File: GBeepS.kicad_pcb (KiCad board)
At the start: 4 copper layers, 10 x 12 mm, 35 parts, among them J1 Ant, U1 NCP160xMX, U2 MMC3416xPJ, U3 ZOE-M8Q, U4 EFM8BB51F16G-A-QFN20, Y1 ECS-.327-7-16-TR3

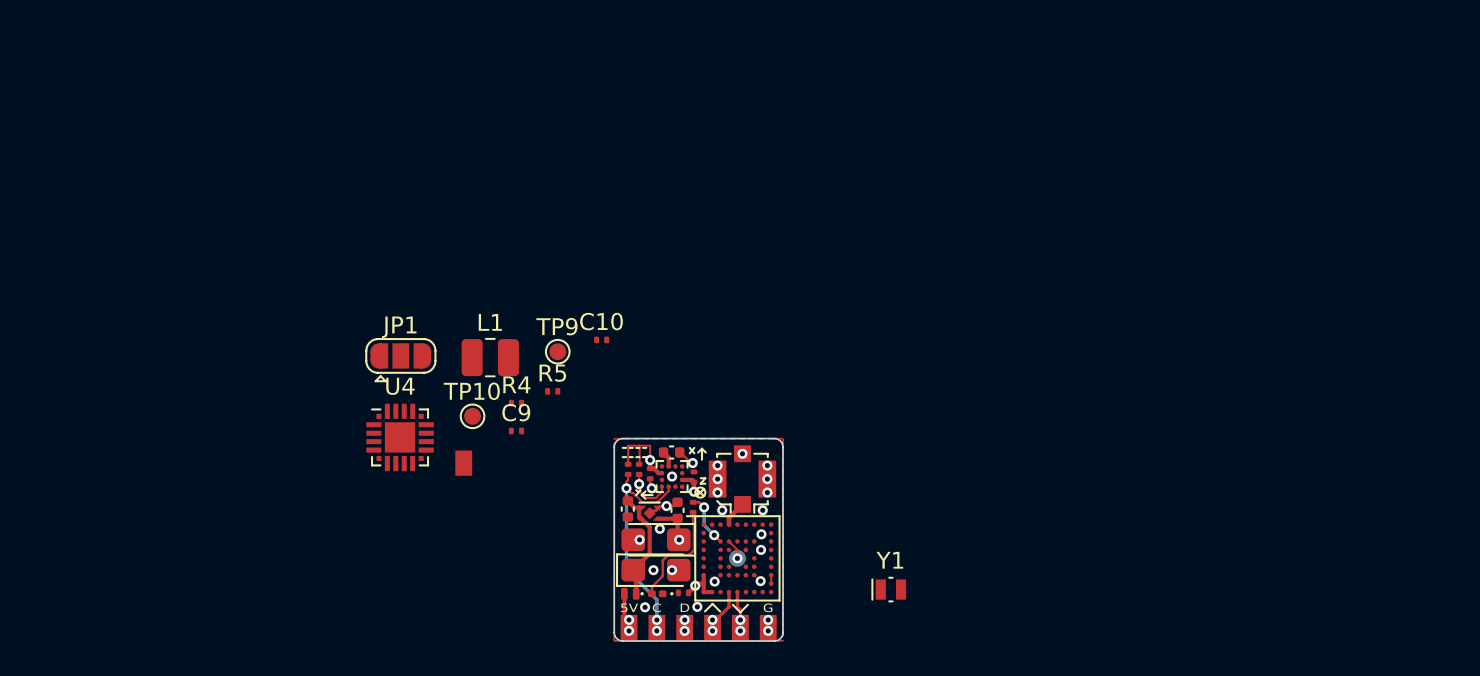
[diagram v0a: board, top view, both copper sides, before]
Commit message: rudimentary layout and 3D models
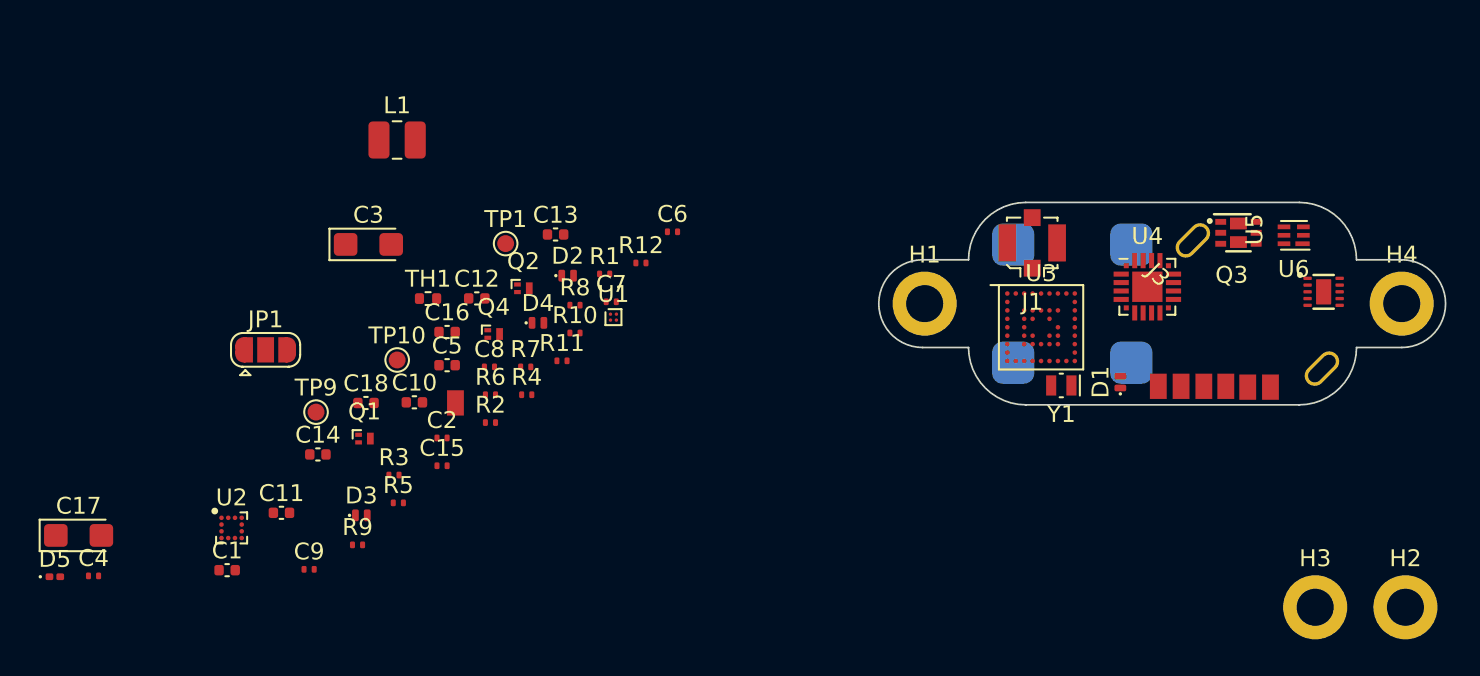
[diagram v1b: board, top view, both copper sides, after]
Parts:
- added C11: 10µF, Capacitor_SMD:C_0402_1005Metric, F.Cu at (80.3, 104.4)
- added C12: 10µF, Capacitor_SMD:C_0402_1005Metric, F.Cu at (91.8, 91.7)
- added C13: 10µF, Capacitor_SMD:C_0402_1005Metric, F.Cu at (96.5, 87.9)
- added C14: 10µF, Capacitor_SMD:C_0402_1005Metric, F.Cu at (82.4, 100.9)
- added C15: 100nF, Yolo-GPS:C_0201_0603Metric_mod, F.Cu at (89.8, 101.6)
- added C16: 10µF, Capacitor_SMD:C_0402_1005Metric, F.Cu at (90.1, 93.7)
- added C17: 100µF, Capacitor_Tantalum_SMD:CP_EIA-3216-18_Kemet-A, F.Cu at (68.2, 105.7)
- added C18: 10µF, Capacitor_SMD:C_0402_1005Metric, F.Cu at (85.3, 97.9)
- added D3: CDBQC0130L-HF, Yolo-GPS:D_SOD-932F_0402_1005Metric, F.Cu at (85.0, 104.5)
- added D4: CDBQC0130L-HF, Yolo-GPS:D_SOD-932F_0402_1005Metric, F.Cu at (95.5, 93.1)
- added D5: green, LED_SMD:LED_0201_0603Metric, F.Cu at (66.8, 108.2)
- added H1: MountingHole, MountingHole:MountingHole_2.2mm_M2_DIN965_Pad, F.Cu at (118.4, 92.0)
- added H2: MountingHole, MountingHole:MountingHole_2.2mm_M2_DIN965_Pad, F.Cu at (146.9, 110.0)
- added H3: MountingHole, MountingHole:MountingHole_2.2mm_M2_DIN965_Pad, F.Cu at (141.6, 110.0)
- added H4: MountingHole, MountingHole:MountingHole_2.2mm_M2_DIN965_Pad, F.Cu at (146.7, 92.0)
- added J2: BAT_TAB_POS, MountingHole:MountingHole_2.2mm_M2_DIN965_Pad, B.Cu at (141.9, 95.8)
- added J3: BAT_TAB_NEGATIVE, MountingHole:MountingHole_2.2mm_M2_DIN965_Pad, F.Cu at (134.3, 88.2)
- added LS1: CMT-85853-97-SMT-TR, Buzzer_Beeper:MagneticBuzzer_CUI_CMT-8504-100-SMT, B.Cu at (127.2, 92.0)
- added Q1: PMZ130UNEYL, Package_DFN_QFN:Diodes_DFN1006-3, F.Cu at (85.2, 100.0)
- added Q2: PMZ130UNEYL, Package_DFN_QFN:Diodes_DFN1006-3, F.Cu at (94.6, 91.1)
- added Q3: DMN1025UFDB, Yolo-GPS:U-DFN2020-6-2EP, F.Cu at (137.0, 87.8)
- added Q4: PMZB320UPE, Package_DFN_QFN:Diodes_DFN1006-3, F.Cu at (92.8, 93.8)
- added R10: 10k, Yolo-GPS:R_0201_0603Metric_mod, F.Cu at (97.7, 93.7)
- added R11: 360R, Yolo-GPS:R_0201_0603Metric_mod, F.Cu at (96.9, 95.4)
- added R12: 300R, Yolo-GPS:R_0201_0603Metric_mod, F.Cu at (101.6, 89.6)
- added R6: 1M, Yolo-GPS:R_0201_0603Metric_mod, F.Cu at (92.7, 97.4)
- added R7: 200k, Yolo-GPS:R_0201_0603Metric_mod, F.Cu at (94.8, 95.8)
- added R8: 100k, Yolo-GPS:R_0201_0603Metric_mod, F.Cu at (97.7, 92.1)
- added R9: 2k2, Yolo-GPS:R_0201_0603Metric_mod, F.Cu at (84.8, 106.3)
- added TH1: NTC 10k, Resistor_SMD:R_0402_1005Metric, F.Cu at (89.0, 91.7)
- added U5: BQ24040, Yolo-GPS:WSON_10_P0.4_2x2, F.Cu at (142.1, 91.3)
- added U6: BQ29700, Package_SON:WSON-6_1.5x1.5mm_P0.5mm, F.Cu at (140.3, 87.9)
- C1: value 1u -> 10µF
- C10: value 1u -> 10µF; footprint Yolo-GPS:C_0201_0603Metric_mod -> Capacitor_SMD:C_0402_1005Metric
- C2: value 1u -> 1µF; footprint Capacitor_SMD:C_0402_1005Metric -> Yolo-GPS:C_0201_0603Metric_mod
- C3: value 100u -> 100µF
- C4, C7, C8, C9: value 1u -> 1µF
- C5: value 4u7 -> 4µ7
- C6: value 100u -> 1nF; footprint Capacitor_Tantalum_SMD:CP_EIA-3216-18_Kemet-A -> Yolo-GPS:C_0201_0603Metric_mod
- D1: value green -> CDBQC0130L-HF; footprint LED_SMD:LED_0201_0603Metric -> Yolo-GPS:D_SOD-932F_0402_1005Metric
- R1: value 360R -> 1M
- R5: value 1k -> 100k
- TP1: moved to F.Cu
- U1: value NCP160xMX -> TCR3UG33A; footprint Yolo-GPS:OnSemi-XDFN-4-1EP_1x1mm_P0.65mm_EP0.52x0.52mm -> Package_BGA:WLP-4_0.73x0.73mm_Layout2x2_P0.35mm_Ball0.22mm_Pad0.2mm_NSMD
- moved U4 45.2 mm to (131.6, 91.0)
- moved TP2 40.6 mm to (138.9, 97.0)
- moved TP4 34.2 mm to (133.6, 96.9)
- moved TP6 33.6 mm to (136.2, 96.9)
- moved C4 33.5 mm to (69.1, 108.1), turned to 0 degrees
- moved TP7 31.8 mm to (137.6, 97.0)
- moved TP3 31.5 mm to (132.2, 96.9)
- moved TP5 31.0 mm to (134.9, 96.9)
- moved D1 30.2 mm to (130.0, 96.7), turned to 90 degrees
- moved U2 26.3 mm to (77.3, 105.3), turned to 0 degrees
- moved C3 24.4 mm to (85.4, 88.5), turned to 0 degrees
- moved C1 24.0 mm to (77.0, 107.8), turned to 0 degrees
- moved TP1 23.2 mm to (93.6, 88.4), turned to 0 degrees
- moved U3 22.6 mm to (125.3, 93.4)
- moved J1 22.2 mm to (124.8, 88.4)
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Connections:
- C1 pad 1: +5V -> BATT_PACK
- C10 pad 1: VSupply_EFM -> VIN
- C6 pad 1: +5V -> BATT_VOL
- C7 pad 1: +3V3 -> Net-(C7-Pad1)
- D1 pad 1: GND -> BATT_PACK
- D2 pad 1: +5V -> VIN
- JP1 pad 3: VSupply_EFM -> +3V3
- R1 pad 1: Net-(R1-Pad1) -> GND
- R1 pad 2: Net-(D1-Pad2) -> Net-(D2-Pad2)
- R4 pad 1: VSupply_EFM -> +3V3
- U3 pad P$C3: Net-(R1-Pad1) -> timepulse
- U3 pad P$H9: VBackup -> +3V3
- U3 pad P$J1: +3V3 -> Net-(C7-Pad1)
- U3 pad P$J2: +3V3 -> Net-(C7-Pad1)
- U4 pad 10: unconnected-(U4-Pad10) -> BATT_VOL
- U4 pad 11: unconnected-(U4-Pad11) -> EN_BATT_VOL
- U4 pad 14: unconnected-(U4-Pad14) -> power_detect
- U4 pad 15: unconnected-(U4-Pad15) -> Net-(U4-Pad15)
- U4 pad 18: unconnected-(U4-Pad18) -> timepulse
- U4 pad 4: VSupply_EFM -> +3V3
- U4 pad 7: unconnected-(U4-Pad7) -> PG
- U4 pad 8: unconnected-(U4-Pad8) -> CHG
- U4 pad 9: unconnected-(U4-Pad9) -> EN_GPA_PWR
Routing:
- net SDA: track 13.7 -> 0.00 mm, vias 3 -> 0
- net SCL: track 13.4 -> 0.00 mm, vias 3 -> 0
- net +3V3: track 12.1 -> 0.00 mm, vias 4 -> 0
- net +5V: track 6.79 -> 0.00 mm
- net Net-(D1-Pad2): track 6.61 -> 0.00 mm
- net GND: track 3.55 -> 0.00 mm, vias 25 -> 0
- net Net-(R1-Pad1): track 3.20 -> 0.00 mm, vias 2 -> 0
- net GNSS_Rx: track 2.82 -> 0.00 mm, vias 2 -> 0
- net Net-(D2-Pad2): track 2.48 -> 0.00 mm, vias 2 -> 0
- net GNSS_Tx: track 2.37 -> 0.00 mm, vias 2 -> 0
- net Net-(J1-Pad1): track 1.53 -> 0.00 mm
- net Net-(TP1-Pad1): track 1.21 -> 0.00 mm, vias 1 -> 0
- net Net-(C5-Pad1): track 0.95 -> 0.00 mm
- net unconnected-(U3-PadP$G9): track 0.50 -> 0.00 mm
- removed copper zone on In2.Cu, net +3V3
- removed copper zone on B.Cu, net GND
- removed copper zone on F.Cu, net GND
- removed copper zone on In1.Cu, net GND
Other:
- board size 10 x 12 mm -> 33.6 x 12 mm
- board text removed: "5V"
- board text removed: "C"
- board text removed: "D"
- board text removed: "G"
- board text removed: "HypaLoc"
- board text removed: "Rev 1.0"
- board text removed: "crteensy"
- board text removed: "safe boot"

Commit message: update layout
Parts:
- TP1: moved to B.Cu
- U1: footprint Package_BGA:WLP-4_0.73x0.73mm_Layout2x2_P0.35mm_Ball0.22mm_Pad0.2mm_NSMD -> Yolo-GPS:WLP-4_0.73x0.73mm_Layout2x2_P0.35mm_Ball0.22mm_Pad0.2mm_NSMD_mod
- moved C17 71.6 mm to (139.0, 94.6), turned to 180 degrees
- moved D5 65.6 mm to (126.8, 81.7)
- moved R9 60.2 mm to (142.2, 88.2), turned to 90 degrees
- moved C18 55.0 mm to (139.5, 88.8), turned to 90 degrees
- moved C1 54.9 mm to (130.6, 95.3)
- moved TH1 54.5 mm to (143.4, 92.6), turned to 90 degrees
- moved C10 53.0 mm to (140.7, 90.9)
- moved C16 52.5 mm to (142.5, 90.9), turned to 180 degrees
- moved C15 52.3 mm to (140.6, 89.3)
- moved TP9 51.6 mm to (133.9, 100.7)
- moved C3 51.3 mm to (136.7, 91.0)
- moved JP1 50.2 mm to (128.7, 103.9)
- moved TP10 49.6 mm to (136.3, 101.2)
- moved D3 47.8 mm to (131.7, 94.2), turned to -90 degrees
- moved Q1 47.1 mm to (130.7, 87.8)
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
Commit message: started routing
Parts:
- removed C8: 1µF, Yolo-GPS:C_0201_0603Metric_mod
- removed H2, H3: MountingHole, MountingHole:MountingHole_2.2mm_M2_DIN965_Pad
- removed JP1: SolderJumper_3_Open, Jumper:SolderJumper-3_P1.3mm_Open_RoundedPad1.0x1.5mm
- added Q5: PMZB320UPE, Package_DFN_QFN:Diodes_DFN1006-3, F.Cu at (127.5, 89.2)
- C7, C9: value 1µF -> 10µF; footprint Yolo-GPS:C_0201_0603Metric_mod -> Capacitor_SMD:C_0402_1005Metric
- L1: value L_Small -> MCHK1608T1R5MKN; footprint Inductor_SMD:L_1008_2520Metric -> Inductor_SMD:L_0603_1608Metric
- TP10, TP9: moved to B.Cu
- moved R3 56.2 mm to (129.8, 87.5), turned to -90 degrees
- moved R2 55.5 mm to (130.1, 88.7), turned to 90 degrees
- moved C4 49.7 mm to (128.4, 86.7), turned to 180 degrees
- moved C5 46.7 mm to (127.0, 87.8), turned to 90 degrees
- moved U2 46.5 mm to (128.4, 87.8), turned to -90 degrees
- moved C14 20.2 mm to (136.2, 94.4), turned to 90 degrees
- moved C13 19.8 mm to (135.3, 94.4), turned to -90 degrees
- moved C12 19.4 mm to (134.5, 94.4), turned to 90 degrees
- moved C11 19.2 mm to (133.7, 94.4), turned to -90 degrees
- moved TP10 17.7 mm to (126.0, 86.8), turned to -90 degrees
- moved TP9 15.3 mm to (127.6, 86.8), turned to -90 degrees
- moved R11 10.8 mm to (132.7, 88.0), turned to 90 degrees
- moved D5 8.08 mm to (133.0, 86.8), turned to 180 degrees
- moved Q4 5.77 mm to (124.2, 97.0), turned to 180 degrees
- moved C9 3.10 mm to (122.6, 93.2), turned to 90 degrees
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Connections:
- C4 pad 1: +3V3 -> Net-(C4-Pad1)
- LS1 pad 3: (no net) -> GND
- LS1 pad 4: (no net) -> GND
- U2 pad 12: +3V3 -> Net-(C4-Pad1)
- U2 pad 6: +3V3 -> Net-(C4-Pad1)
- U4 pad 1: Net-(JP1-Pad2) -> unconnected-(U4-Pad1)
- U4 pad 13: unconnected-(U4-Pad13) -> PG
- U4 pad 14: power_detect -> CHG
- U4 pad 17: unconnected-(U4-Pad17) -> SCL
- U4 pad 18: timepulse -> EN_PWR_MAG
- U4 pad 19: unconnected-(U4-Pad19) -> Buzz_out
- U4 pad 20: Buzz_out -> SDA
- U4 pad 7: PG -> timepulse
- U4 pad 8: CHG -> power_detect
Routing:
- net GND: track 0.00 -> 29.6 mm, vias 0 -> 39
- net SDA: track 0.00 -> 15.5 mm, vias 0 -> 2
- net BATT_PACK: track 0.00 -> 14.6 mm, vias 0 -> 1
- net SCL: track 0.00 -> 14.4 mm, vias 0 -> 3
- net C2D: track 0.00 -> 14.4 mm, vias 0 -> 1
- net EN_GPA_PWR: track 0.00 -> 13.9 mm, vias 0 -> 2
- net GNSS_Rx: track 0.00 -> 13.9 mm, vias 0 -> 3
- net Net-(D2-Pad2): track 0.00 -> 12.8 mm
- net GNSS_Tx: track 0.00 -> 11.7 mm, vias 0 -> 3
- net +3V3: track 0.00 -> 10.6 mm, vias 0 -> 14
- net Net-(R5-Pad1): track 0.00 -> 8.12 mm
- net timepulse: track 0.00 -> 7.90 mm, vias 0 -> 2
- net C2CK: track 0.00 -> 7.29 mm, vias 0 -> 1
- net BATT_VOL: track 0.00 -> 5.63 mm
- net EN_BATT_VOL: track 0.00 -> 4.60 mm
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- added copper zone on In2.Cu, net +3V3
- added copper zone on In1.Cu, net GND
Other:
- board text added: "C14"

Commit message: added pushbutton and routed everything
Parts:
- added SW1: EVP-AKE31A, Yolo-GPS:EVPAV, F.Cu at (143.0, 87.0)
- moved D1 8.49 mm to (130.7, 95.3), turned to 90 degrees
- moved C6 6.36 mm to (131.6, 88.2), turned to 0 degrees
- moved Q1 6.05 mm to (130.5, 94.0), turned to -90 degrees
- moved TH1 2.34 mm to (142.4, 94.7), turned to 180 degrees
- moved R6 1.96 mm to (132.7, 95.0), turned to -90 degrees
- moved R9 1.77 mm to (140.4, 88.7), turned to -90 degrees
- moved C15 1.73 mm to (138.9, 89.0)
- moved U6 1.68 mm to (139.2, 87.5)
- moved R7 1.35 mm to (137.8, 92.0)
- moved C18 1.20 mm to (139.8, 90.0), turned to 180 degrees
- moved Q3 1.10 mm to (136.7, 87.9)
- moved R1 0.85 mm to (132.7, 93.8), turned to -90 degrees
- moved D3 0.78 mm to (131.7, 94.6), turned to 90 degrees
- moved R12 0.73 mm to (141.3, 89.8), turned to 90 degrees
- moved LS1 0.22 mm to (126.8, 92.1), turned to 180 degrees
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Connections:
- U4 pad 10: BATT_VOL -> power_detect
- U4 pad 16: unconnected-(U4-Pad16) -> SW
- U4 pad 19: Buzz_out -> BATT_VOL
- U4 pad 8: power_detect -> Buzz_out
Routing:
- net BATT_PACK: track 14.6 -> 43.6 mm, vias 1 -> 3
- net EN_PWR_MAG: track 0.00 -> 19.0 mm, vias 0 -> 2
- net VIN: track 0.52 -> 17.8 mm, vias 1 -> 2
- net Net-(C15-Pad1): track 0.00 -> 12.7 mm
- net GND: track 29.6 -> 41.6 mm, vias 39 -> 58
- net CHG: track 0.00 -> 11.9 mm, vias 0 -> 2
- net SW: track 0.00 -> 11.8 mm, vias 0 -> 4
- net BATT_VOL: track 5.63 -> 16.6 mm, vias 0 -> 4
- net PG: track 0.00 -> 8.35 mm, vias 0 -> 2
- net SDA: track 15.5 -> 23.3 mm, vias 2 -> 4
- net TS: track 0.00 -> 4.58 mm
- net Net-(Q3-Pad5): track 0.00 -> 4.31 mm
- net Net-(Q3-Pad3): track 0.00 -> 3.28 mm
- net Net-(Q3-Pad2): track 0.00 -> 3.28 mm
- net Net-(C15-Pad2): track 0.00 -> 3.25 mm
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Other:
- outline, holes or cut-outs redrawn
